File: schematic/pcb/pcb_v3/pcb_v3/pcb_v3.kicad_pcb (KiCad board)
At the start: 4 copper layers, 56 x 67 mm, 58 parts, among them IC1 FT232RNQ-TRAY, J1 5V, J2 SERVO, J3 MAVLINK, J4 DISPLAY, J5 SER. SERVO, J6 MAG., J7 U.FL-R, J8 Conn_01x05_Pin, J9 Conn_01x05_Pin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

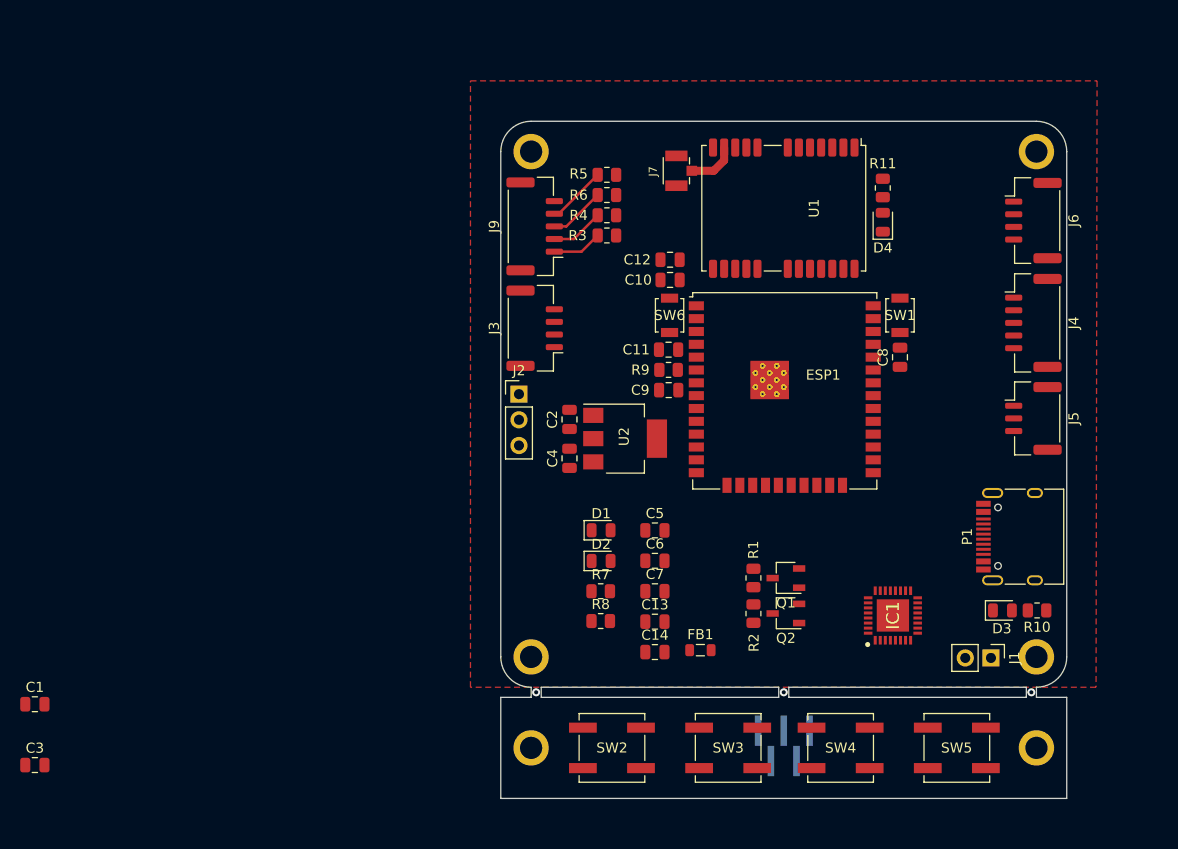
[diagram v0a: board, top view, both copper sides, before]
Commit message: pcb update, bluetooth bridge working
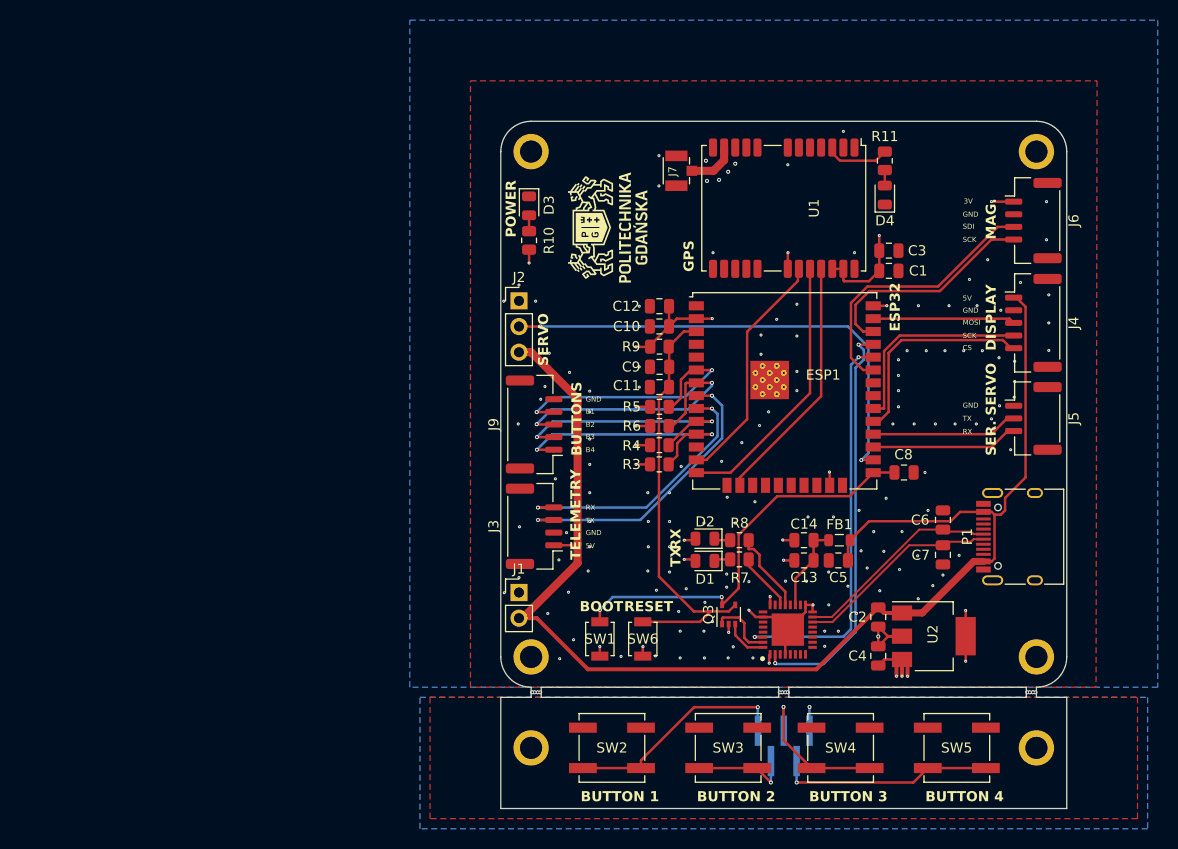
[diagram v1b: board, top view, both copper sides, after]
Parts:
- removed Q1, Q2: NPN, Package_TO_SOT_SMD:TSOT-23
- removed R1, R2: 10K, Resistor_SMD:R_0805_2012Metric
- added G***: LOGO, LOGO, F.Cu at (197.6, 57.5)
- added Q3: UMG8NTR, Package_TO_SOT_SMD:SOT-353_SC-70-5, F.Cu at (209.6, 95.8)
- moved C3 98.6 mm to (225.4, 59.8)
- moved C1 94.8 mm to (225.4, 61.8)
- moved R10 62.2 mm to (189.8, 58.8), turned to 90 degrees
- moved D3 61.6 mm to (189.8, 55.4), turned to -90 degrees
- moved J1 47.1 mm to (188.8, 93.6), turned to 0 degrees
- moved SW1 43.7 mm to (196.8, 98.2), turned to 90 degrees
- moved C4 36.3 mm to (224.3, 99.9)
- moved C2 36.3 mm to (224.3, 96.0)
- moved U2 36.3 mm to (229.8, 98.0)
- moved SW6 32.1 mm to (201.1, 98.2), turned to 90 degrees
- moved C6 28.8 mm to (230.8, 86.5), turned to 90 degrees
- moved C7 28.7 mm to (230.8, 89.9), turned to -90 degrees
- moved R5 23.5 mm to (202.7, 75.2), turned to 0 degrees
- moved R6 23.4 mm to (202.7, 77.2), turned to 0 degrees
- moved R4 23.3 mm to (202.7, 79.0), turned to 0 degrees
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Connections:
- ESP1 pad 10: BUTTON_1_ESP -> BUTTON_2_ESP
- ESP1 pad 11: BUTTON_2_ESP -> BUTTON_1_ESP
- ESP1 pad 6: BUTTON_3_ESP -> BUTTON_4_ESP
- ESP1 pad 7: BUTTON_4_ESP -> BUTTON_3_ESP
- IC1 pad 33: unconnected-(IC1-EP-Pad33) -> GND
- J3 pad 3: MAV_RX -> MAV_TX
- J3 pad 4: MAV_TX -> MAV_RX
- J4 pad 3: SCREEN_SCK -> SCREEN_MOSI
- J4 pad 4: SCREEN_MOSI -> SCREEN_SCK
- J5 pad 2: SERVO_RX -> SERVO_TX
- J5 pad 3: SERVO_TX -> SERVO_RX
- J8 pad 5: GND -> GND1
- SW2 pad 1: GND -> GND1
- SW3 pad 1: GND -> GND1
- SW4 pad 1: GND -> GND1
- SW5 pad 1: GND -> GND1
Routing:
- net +5V: track 0.00 -> 134.3 mm
- net SERVO: track 0.00 -> 48.1 mm, vias 0 -> 2
- net EN: track 0.00 -> 42.9 mm
- net +3V3: track 0.00 -> 40.9 mm, vias 0 -> 15
- net ESP32_TX0: track 0.00 -> 40.6 mm, vias 0 -> 2
- net IO0: track 0.00 -> 40.1 mm, vias 0 -> 2
- net ESP32_RX0: track 0.00 -> 39.3 mm, vias 0 -> 2
- net GND: track 0.00 -> 29.7 mm, vias 0 -> 154
- net MAV_TX: track 0.00 -> 29.3 mm, vias 0 -> 2
- net MAG_SDI: track 0.00 -> 27.3 mm
- net GPS_MISO: track 0.00 -> 26.8 mm
- net MAV_RX: track 0.00 -> 26.8 mm, vias 0 -> 2
- net GPS_CS: track 0.00 -> 26.3 mm, vias 0 -> 2
- net GPS_MOSI: track 0.00 -> 24.8 mm
- net GPS_SCK: track 0.00 -> 23.7 mm
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- added copper zone on B.Cu, net GND
- added copper zone on B.Cu, net GND1
- added copper zone on F.Cu, net GND1
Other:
- board size 56 x 67 mm -> 56 x 68 mm
- board text added: "3V"
- board text added: "5V"
- board text added: "B1"
- board text added: "B2"
- board text added: "B3"
- board text added: "B4"
- board text added: "BOOT"
- board text added: "BUTTON 1"
- board text added: "BUTTON 2"
- board text added: "BUTTON 3"
- board text added: "BUTTON 4"
- board text added: "BUTTONS"
- board text added: "CS"
- board text added: "DISPLAY"
- board text added: "ESP32"
- board text added: "GND"
- board text added: "GPS"
- board text added: "JLCJLCJLCJLC"
- board text added: "MAG."
- board text added: "MOSI"
- board text added: "POWER"
- board text added: "RESET"
- board text added: "RX"
- board text added: "SCK"
- board text added: "SDI"
- board text added: "SER. SERVO"
- board text added: "SERVO"
- board text added: "TELEMETRY"
- board text added: "TRACKER PCB v. beta 5/2024"
- board text added: "TX"

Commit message: pcb updates
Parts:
- removed J8: Conn_01x05_Pin, Connector_PinHeader_1.27mm:PinHeader_1x05_P1.27mm_Vertical_SMD_Pin1Left
- removed Q3: UMG8NTR, Package_TO_SOT_SMD:SOT-353_SC-70-5
- removed the REF** at (190.0, 109.0)
- removed the REF** at (240.0, 109.0)
- removed SW2, SW3, SW4, SW5: SW_Push, Button_Switch_SMD:SW_SPST_B3SL-1002P
- added BT1: Battery_Cell, Battery:BatteryHolder_Keystone_1060_1x2032, B.Cu at (215.2, 59.5)
- added C15: 0.1uF, Capacitor_SMD:C_0805_2012Metric, F.Cu at (220.4, 92.5)
- added Q1: NPN, Package_TO_SOT_SMD:TSOT-23, F.Cu at (209.0, 99.0)
- added Q2: NPN, Package_TO_SOT_SMD:TSOT-23, F.Cu at (209.0, 95.6)
- added R1: 10K, Resistor_SMD:R_0805_2012Metric, F.Cu at (205.2, 95.6)
- added R2: 10K, Resistor_SMD:R_0805_2012Metric, F.Cu at (205.2, 99.0)
- C11, C8: value 0.1uF -> 47pF
- C2, C4: value 10uF -> 1uF
- moved G*** 1.03 mm to (197.3, 56.5)
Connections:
- IC1 pad 16: GND -> Net-(IC1-3V3OUT)
- U1 pad 22: +3V3 -> Net-(BT1-+)
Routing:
- net BUTTON_1: track 22.6 -> 0.00 mm, vias 1 -> 0
- net BUTTON_4: track 21.4 -> 0.00 mm, vias 1 -> 0
- net BUTTON_3: track 15.3 -> 0.00 mm, vias 1 -> 0
- net Net-(BT1-+): track 0.00 -> 12.5 mm, vias 0 -> 1
- net DTR: track 6.53 -> 16.6 mm
- net BUTTON_2: track 9.86 -> 0.00 mm, vias 1 -> 0
- net GND: track 29.7 -> 35.5 mm, vias 154 -> 60
- net ESP32_RX0: track 39.3 -> 34.6 mm
- net RTS: track 4.35 -> 8.87 mm
- net Net-(IC1-3V3OUT): track 0.00 -> 3.76 mm
- net Net-(Q2-B): track 0.00 -> 3.25 mm
- net EN: track 42.9 -> 40.0 mm
- net Net-(Q1-B): track 0.00 -> 2.49 mm
- net ESP32_TX0: track 40.6 -> 38.2 mm
- net GND1: track 2.35 -> 0.00 mm, vias 1 -> 0
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- removed copper zone on B.Cu, net GND1
- removed copper zone on F.Cu, net GND1
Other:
- board size 56 x 68 mm -> 56 x 56 mm
- board text added: "5V IN"
- board text added: "TRACKER PCB v. beta v3 6/2024"
- board text removed: "BUTTON 1"
- board text removed: "BUTTON 2"
- board text removed: "BUTTON 3"
- board text removed: "BUTTON 4"
- board text removed: "TRACKER PCB v. beta 5/2024"
